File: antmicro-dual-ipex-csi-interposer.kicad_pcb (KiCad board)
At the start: 4 copper layers, 26.5 x 35.5 mm, 18 parts, among them J1 WE_68715014522, J2 MSAK24025P30

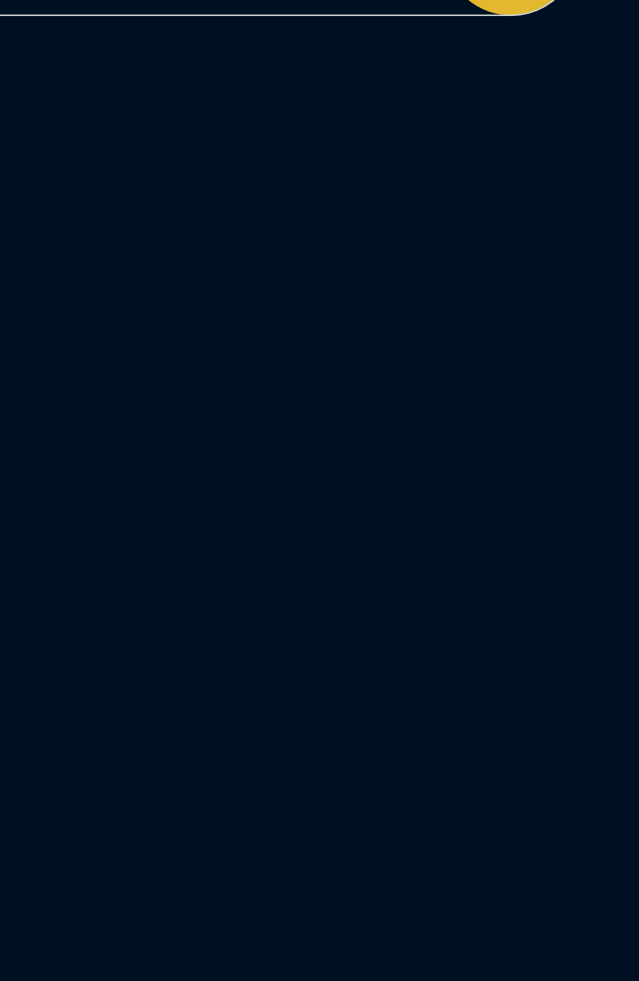
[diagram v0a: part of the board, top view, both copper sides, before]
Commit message: Add second connector and assigned signals
Remove Kicad5 CI
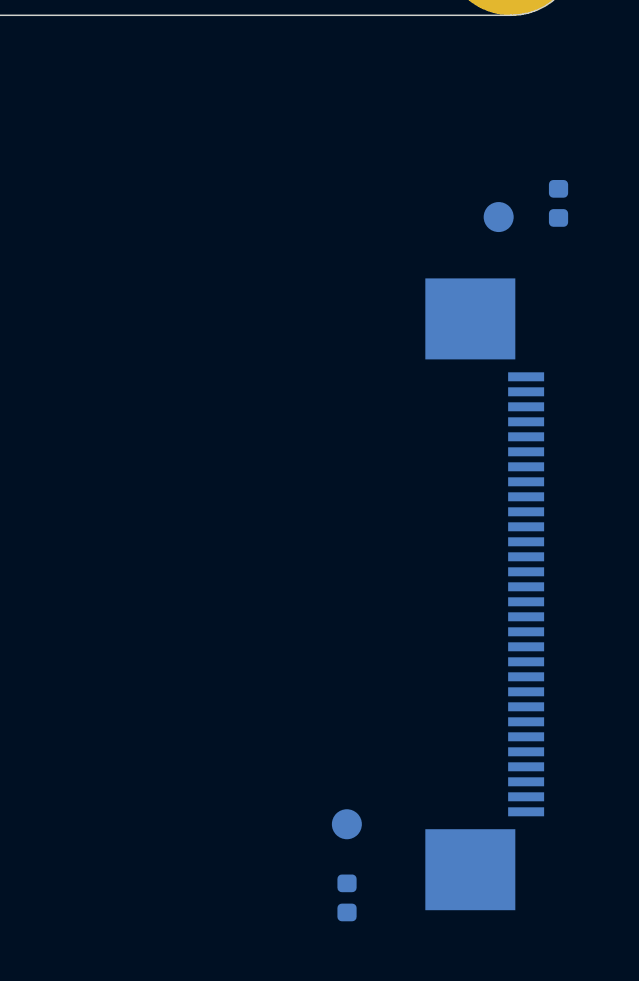
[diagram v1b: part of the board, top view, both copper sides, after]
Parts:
- added J3: MSAK24025P30, antmicro-footprints:MSAK24025P30, B.Cu at (125.4, 154.8)
- added R3: R_0R_0402, antmicro-footprints:0402-res, B.Cu at (118.8, 164.9)
- added R4: R_0R_0402, antmicro-footprints:0402-res, B.Cu at (125.8, 141.8)
- added TP10: TP_SMD1MM, antmicro-footprints:Testpoint_smd_1mm, B.Cu at (123.8, 142.2)
- added TP9: TP_SMD1MM, antmicro-footprints:Testpoint_smd_1mm, B.Cu at (118.7, 162.5)
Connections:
- net CSI_CAM_EN renamed CAM1_CSI_CAM_EN
- net CSI_CAM_XVS renamed CAM1_CSI_CAM_XVS
- net CSI_CLK_N renamed CAM1_CSI_CLK_N
- net CSI_CLK_P renamed CAM1_CSI_CLK_P
- net CSI_D0_N renamed CAM1_CSI_D0_N
- net CSI_D0_P renamed CAM1_CSI_D0_P
- net CSI_D1_N renamed CAM1_CSI_D1_N
- net CSI_D1_P renamed CAM1_CSI_D1_P
- net CSI_D2_N renamed CAM1_CSI_D2_N
- net CSI_D2_P renamed CAM1_CSI_D2_P
- net CSI_D3_N renamed CAM1_CSI_D3_N
- net CSI_D3_P renamed CAM1_CSI_D3_P
- J1 pad 1: unconnected-(J1-Pad1) -> CAM2_CSI_D3_N
- J1 pad 10: unconnected-(J1-Pad10) -> CAM2_CSI_CLK_N
- J1 pad 11: unconnected-(J1-Pad11) -> CAM2_CSI_CLK_P
- J1 pad 2: unconnected-(J1-Pad2) -> CAM2_CSI_D3_P
- J1 pad 3: unconnected-(J1-Pad3) -> CAM2_CSI_D2_N
- J1 pad 4: unconnected-(J1-Pad4) -> CAM2_CSI_D2_P
- J1 pad 5: unconnected-(J1-Pad5) -> CAM2_CSI_D1_N
- J1 pad 6: unconnected-(J1-Pad6) -> CAM2_CSI_D1_P
- J1 pad 7: unconnected-(J1-Pad7) -> CAM2_CSI_D0_N
- J1 pad 8: unconnected-(J1-Pad8) -> CAM2_CSI_D0_P
- J2 pad 22: CSI_CAM_CLK -> CAM1_CSI_CAM_CLK
- J2 pad 23: CSI_CAM_XTRIG -> CAM1_CSI_CAM_XTRIG
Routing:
- net CSI_CAM_XTRIG: track 30.1 -> 0.00 mm
- net CAM1_CSI_CAM_XTRIG: track 0.00 -> 30.1 mm
- net CSI_CAM_CLK: track 28.0 -> 0.00 mm
- net CAM1_CSI_CAM_CLK: track 0.00 -> 28.0 mm

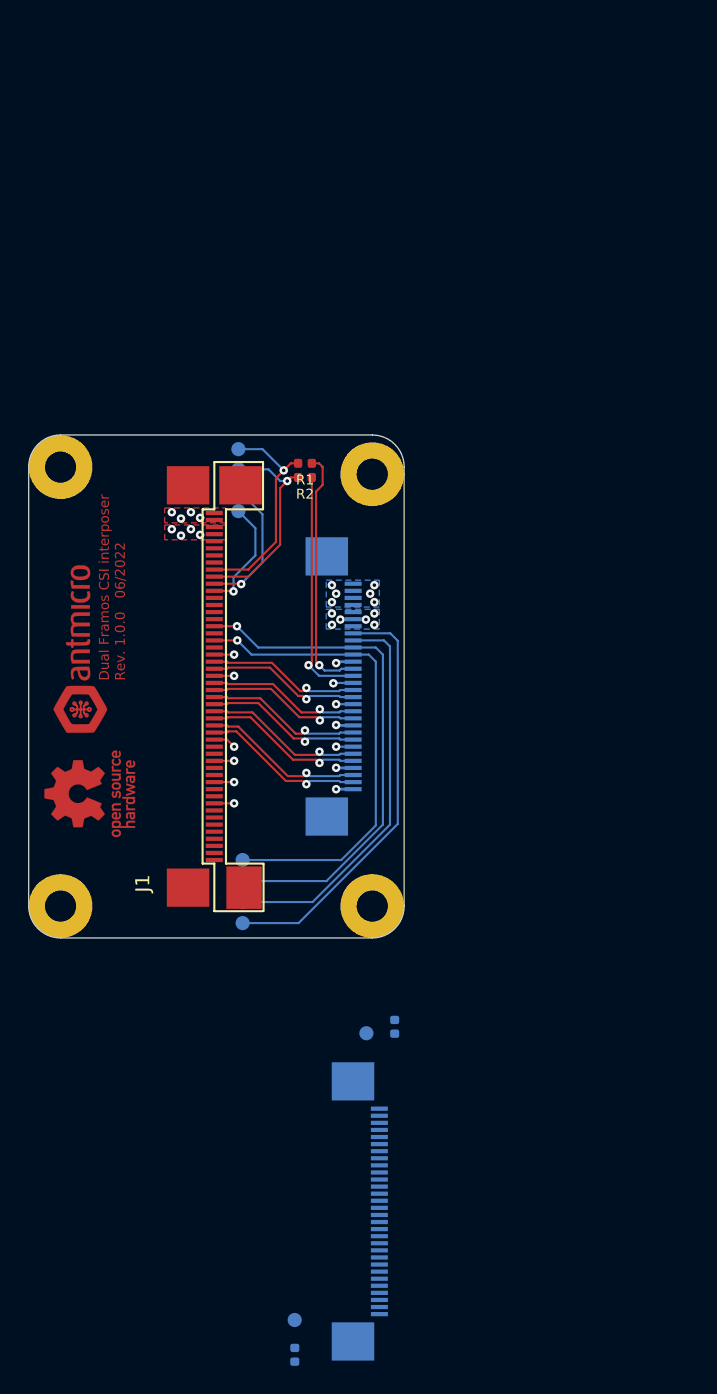
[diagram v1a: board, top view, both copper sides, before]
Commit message: Complete schematic. Proceed PCB layout
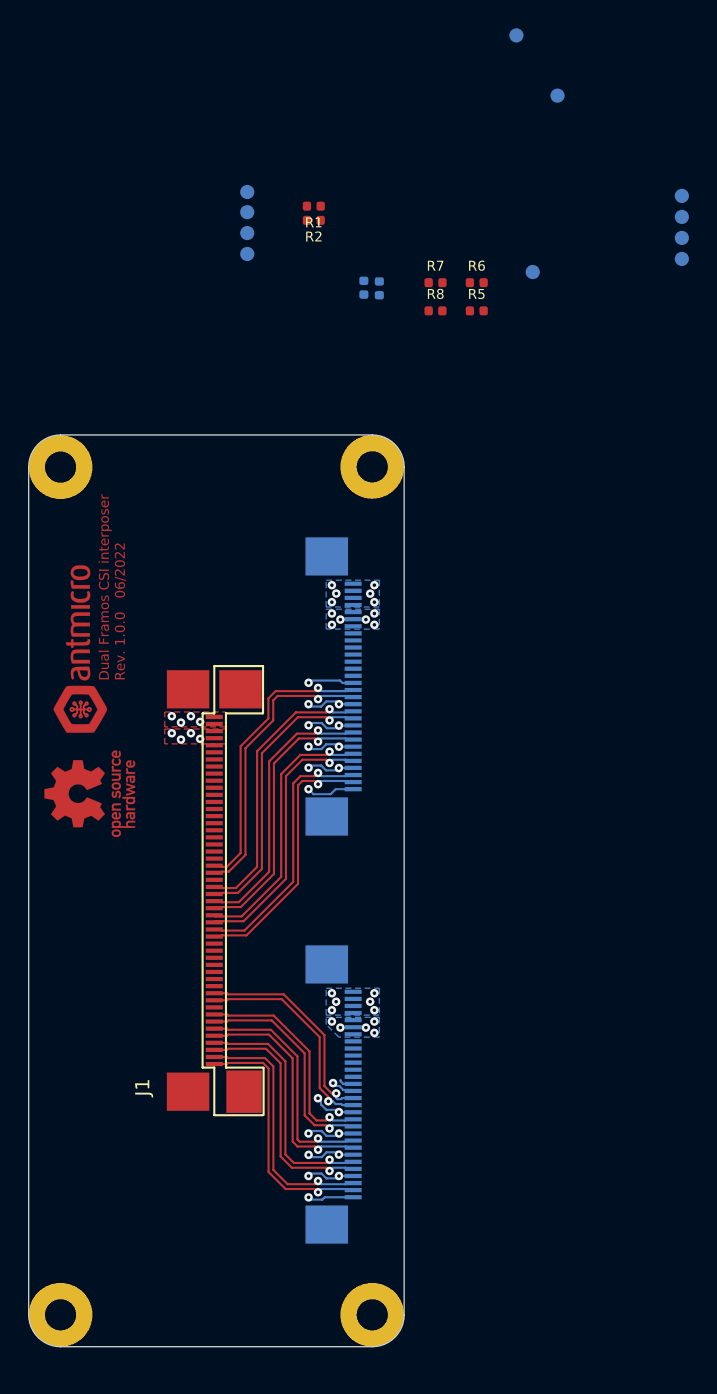
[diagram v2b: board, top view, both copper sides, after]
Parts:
- added R5: R_0R_0402, antmicro-footprints:0402-res, F.Cu at (131.6, 91.2)
- added R6: R_0R_0402, antmicro-footprints:0402-res, F.Cu at (131.6, 89.2)
- added R7: R_0R_0402, antmicro-footprints:0402-res, F.Cu at (128.7, 89.2)
- added R8: R_0R_0402, antmicro-footprints:0402-res, F.Cu at (128.7, 91.2)
- added TP3: TP_SMD1MM, antmicro-footprints:Testpoint_smd_1mm, B.Cu at (134.4, 71.8)
- moved TP9 75.8 mm to (135.5, 88.5)
- moved R3 75.5 mm to (123.7, 89.6)
- moved TP10 67.5 mm to (137.3, 76.0)
- moved TP2 56.2 mm to (146.1, 87.5)
- moved TP8 56.2 mm to (146.1, 84.6)
- moved TP1 56.2 mm to (146.1, 86.0)
- moved TP7 56.2 mm to (146.1, 83.1)
- moved R4 52.1 mm to (124.8, 89.7)
- moved MP2 28.8 mm to (102.2, 162.1)
- moved MP4 28.8 mm to (124.2, 162.1)
- moved R1 18.2 mm to (120.1, 83.8)
- moved R2 18.2 mm to (120.1, 84.8)
- moved TP4 18.2 mm to (115.4, 85.8)
- moved TP3 18.2 mm to (115.4, 87.3)
- moved TP5 18.2 mm to (115.4, 82.9)
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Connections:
- J1 pad 32: CAM1_CSI_CAM_EN -> /CAM_CSI_CAM_EN
- J1 pad 34: CAM1_CSI_CAM_XVS -> /CAM_CSI_CAM_XVS
- J3 pad 20: CAM1_CSI_CAM_EN -> CAM2_CSI_CAM_EN
- J3 pad 21: CAM1_CSI_CAM_XVS -> CAM2_CSI_CAM_XVS
- J3 pad 22: CAM1_CSI_CAM_CLK -> CAM2_CSI_CAM_CLK
- J3 pad 23: CAM1_CSI_CAM_XTRIG -> CAM2_CSI_CAM_XTRIG
- TP7 pad 1: CAM1_CSI_CAM_EN -> /CAM_CSI_CAM_EN
- TP8 pad 1: CAM1_CSI_CAM_XVS -> /CAM_CSI_CAM_XVS
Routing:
- net CAM1_CSI_CAM_XVS: track 36.3 -> 0.00 mm, vias 1 -> 0
- net CAM1_CSI_CAM_EN: track 34.0 -> 0.00 mm, vias 1 -> 0
- net CAM1_CSI_CAM_XTRIG: track 30.1 -> 0.00 mm
- net CAM1_CSI_CAM_CLK: track 28.0 -> 0.00 mm
- net GND: track 17.3 -> 38.7 mm, vias 13 -> 20
- net CAM2_CSI_D3_N: track 0.00 -> 18.0 mm, vias 0 -> 1
- net CAM2_CSI_D3_P: track 0.00 -> 18.0 mm, vias 0 -> 1
- net CAM1_SCL: track 17.8 -> 0.00 mm, vias 1 -> 0
- net CAM2_CSI_D2_N: track 0.00 -> 17.4 mm, vias 0 -> 1
- net CAM2_CSI_D2_P: track 0.00 -> 17.4 mm, vias 0 -> 1
- net CAM1_SDA: track 16.8 -> 0.00 mm, vias 1 -> 0
- net CAM2_CSI_D1_N: track 0.00 -> 16.8 mm, vias 0 -> 1
- net CAM2_CSI_D1_P: track 0.00 -> 16.8 mm, vias 0 -> 1
- net CAM2_CSI_D0_N: track 0.00 -> 15.7 mm, vias 0 -> 1
- net CAM2_CSI_D0_P: track 0.00 -> 15.7 mm, vias 0 -> 1
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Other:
- board size 26.5 x 35.5 mm -> 26.5 x 64.3 mm

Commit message: Route low speed, optimize polygons, match lane length
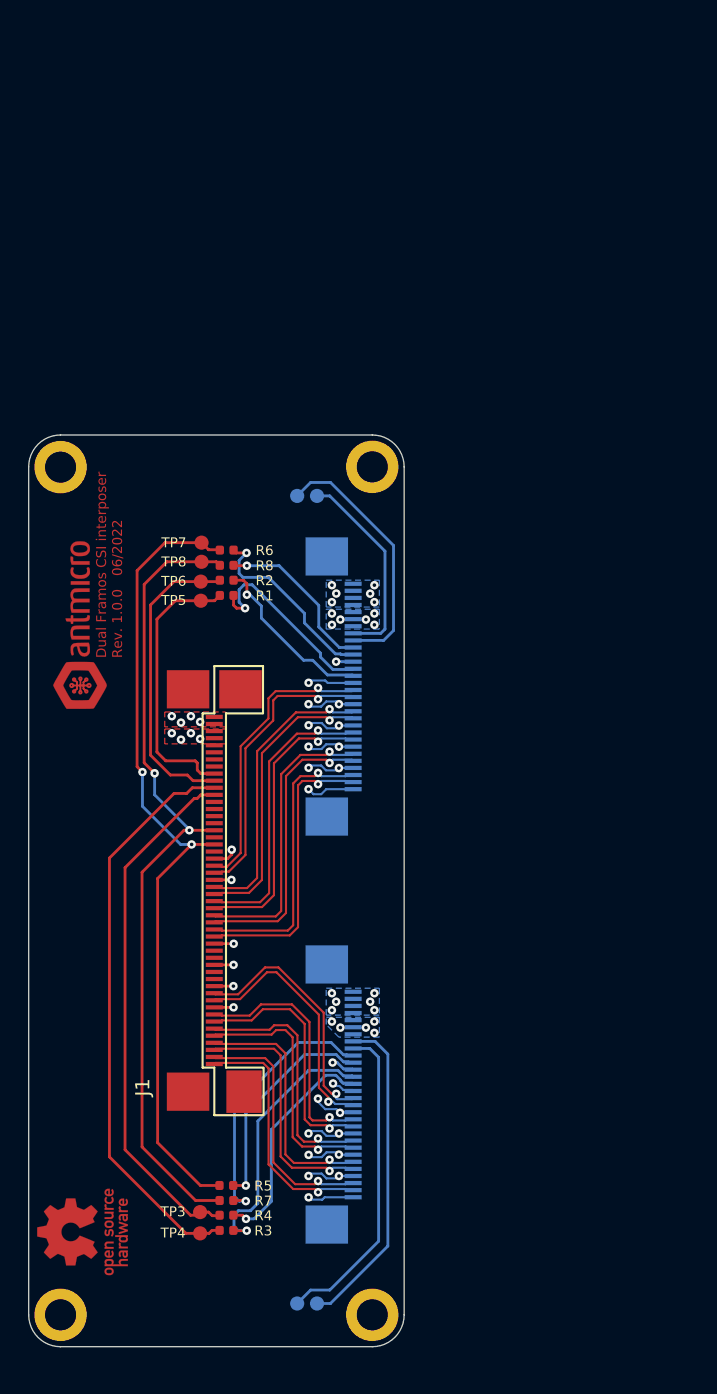
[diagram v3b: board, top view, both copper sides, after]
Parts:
- removed the TP3 at (134.4, 71.8)
- R3, R4, TP3, TP4, TP5, TP6, TP7, TP8: moved to F.Cu
- moved TP10 86.9 mm to (120.3, 161.3)
- moved TP9 74.7 mm to (118.9, 161.3)
- moved TP4 70.7 mm to (112.1, 156.4), turned to 0 degrees
- moved TP3 67.7 mm to (112.1, 154.9), turned to 0 degrees
- moved R3 67.2 mm to (114.0, 156.1), turned to 180 degrees
- moved R7 66.4 mm to (114.0, 154.0), turned to 180 degrees
- moved R4 66.3 mm to (114.0, 155.1), turned to 180 degrees
- moved R5 64.2 mm to (114.0, 153.0), turned to 180 degrees
- moved TP7 41.8 mm to (112.2, 107.5), turned to 180 degrees
- moved TP8 41.7 mm to (112.2, 108.9), turned to 180 degrees
- moved TP1 32.7 mm to (119.0, 104.2)
- moved N1 30.9 mm to (103.8, 156.2)
- moved TP2 30.7 mm to (120.3, 104.2)
- moved TP5 29.0 mm to (112.2, 111.8), turned to 0 degrees
- moved R1 28.2 mm to (114.0, 111.3)
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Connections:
- TP1 pad 1: CSI_CAM_CLK -> CAM1_CSI_CAM_CLK
- TP10 pad 1: CSI_CAM_XTRIG -> CAM2_CSI_CAM_XTRIG
- TP2 pad 1: CSI_CAM_XTRIG -> CAM1_CSI_CAM_XTRIG
- TP9 pad 1: CSI_CAM_CLK -> CAM2_CSI_CAM_CLK
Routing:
- net /CAM_CSI_CAM_XVS: track 0.00 -> 57.5 mm, vias 0 -> 2
- net /CAM_CSI_CAM_EN: track 0.00 -> 57.5 mm, vias 0 -> 2
- net /CAM_L_SCL: track 0.00 -> 40.6 mm
- net /CAM_L_SDA: track 0.00 -> 37.0 mm
- net CAM2_CSI_CAM_XTRIG: track 0.00 -> 23.0 mm
- net CAM2_CSI_CAM_CLK: track 0.00 -> 22.6 mm
- net /CAM_R_SDA: track 0.00 -> 21.5 mm
- net /CAM_R_SCL: track 0.00 -> 19.5 mm
- net CAM2_SCL: track 0.00 -> 19.0 mm, vias 0 -> 1
- net CAM2_CSI_CAM_XVS: track 0.00 -> 18.8 mm, vias 0 -> 1
- net CAM1_CSI_CAM_CLK: track 0.00 -> 18.2 mm
- net CAM2_CSI_CAM_EN: track 0.00 -> 15.5 mm, vias 0 -> 1
- net CAM2_SDA: track 1.06 -> 16.0 mm, vias 0 -> 1
- net CAM1_CSI_CAM_XTRIG: track 0.00 -> 14.3 mm
- net CAM1_SCL: track 0.00 -> 13.9 mm, vias 0 -> 1
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- added copper zone on In2.Cu, net 5V0_SYS

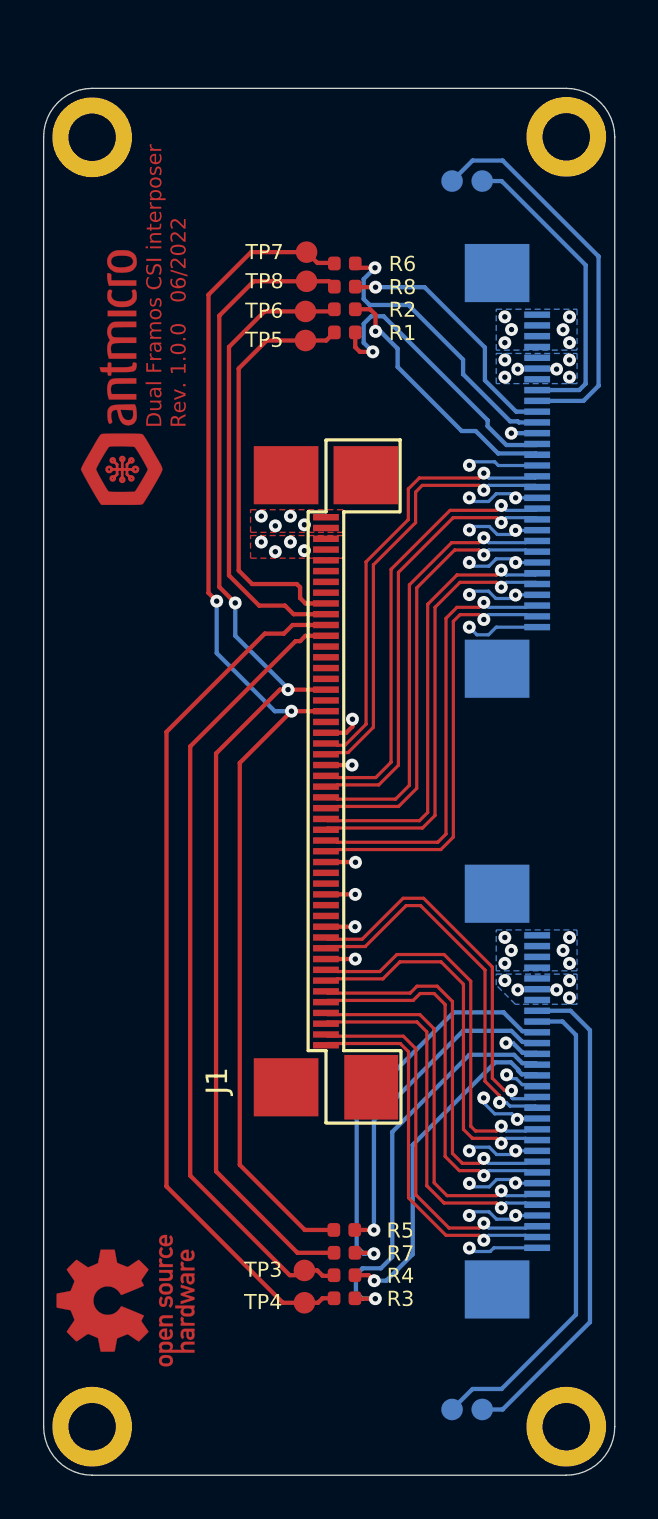
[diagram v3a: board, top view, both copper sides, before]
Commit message: Add decoupling, move all TP to the top
Cosmetic changes

Capital letter fix
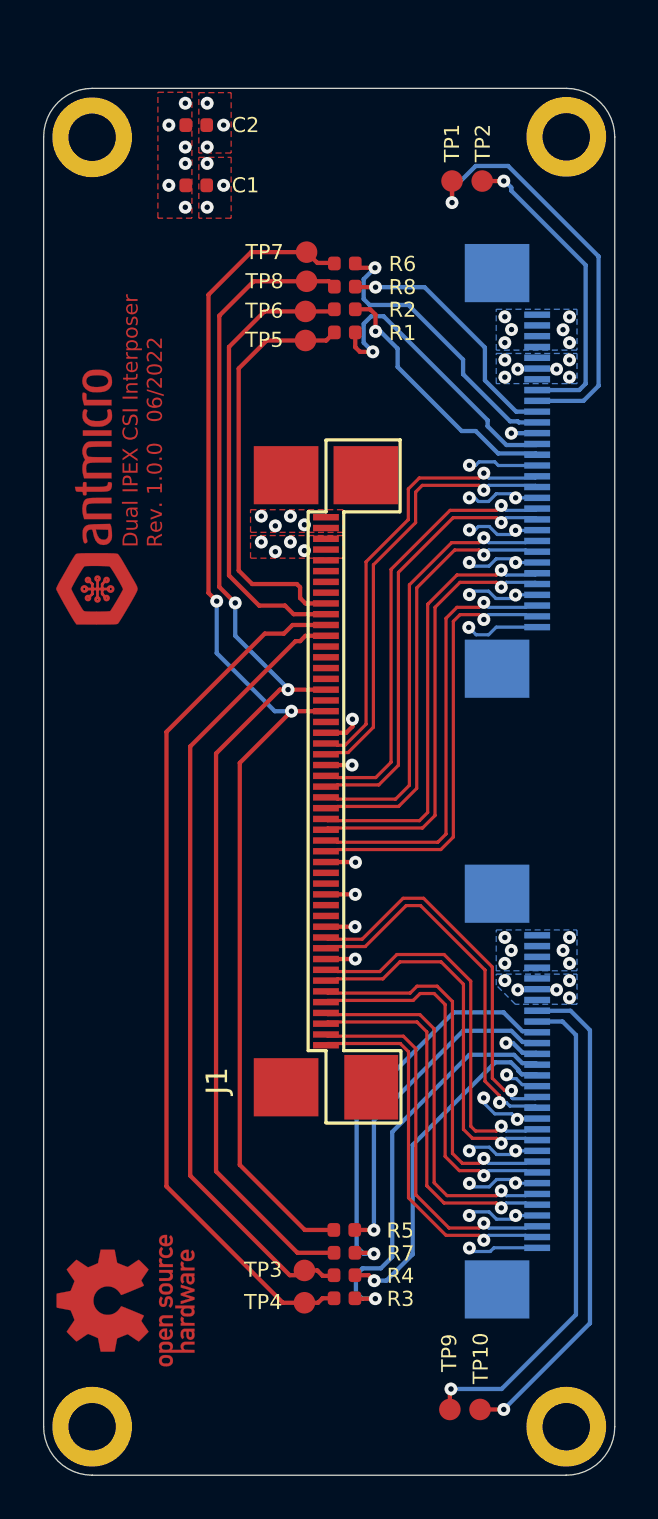
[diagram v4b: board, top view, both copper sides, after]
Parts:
- added C1: C_100n_0402, antmicro-footprints:0402-cap, F.Cu at (107.1, 104.5)
- added C2: C_100n_0402, antmicro-footprints:0402-cap, F.Cu at (107.1, 101.7)
- TP1, TP10, TP2, TP9: moved to F.Cu
- moved N2 5.67 mm to (102.5, 119.0)
- turned TP1 to 180 degrees
- turned TP2 to 180 degrees
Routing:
- net CAM1_CSI_CAM_CLK: track 18.2 -> 19.7 mm, vias 0 -> 1
- net CAM2_CSI_CAM_CLK: track 22.6 -> 23.2 mm, vias 0 -> 1
- net CAM2_CSI_CAM_XTRIG: track 23.0 -> 23.2 mm, vias 0 -> 1
- net CAM1_CSI_CAM_XTRIG: track 14.3 -> 14.4 mm, vias 0 -> 1
- net GND: track 49.9 -> 50.0 mm, vias 28 -> 34
- net 5V0_SYS: vias 16 -> 19
- net 3V3_FFC: vias 15 -> 18
- added copper zone on F.Cu, net GND
- added copper zone on In1.Cu, net GND
- removed copper zone on In1.Cu, net 5V0_SYS
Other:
- board text added: "Dual IPEX CSI Interposer Rev. 1.0.0 06/2022"
- board text removed: "Dual Framos CSI interposer Rev. 1.0.0 06/2022"

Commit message: Generate loclib. Cleanup
Add boards image. Add image link to README
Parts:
- C1, C2: footprint antmicro-footprints:0402-cap -> antmicro-dual-ipex-csi-interposer-footprints:0402-cap
- J1: footprint antmicro-footprints:WE_68715014522 -> antmicro-dual-ipex-csi-interposer-footprints:WE_68715014522
- J2, J3: footprint antmicro-footprints:MSAK24025P30 -> antmicro-dual-ipex-csi-interposer-footprints:MSAK24025P30
- MP1, MP2, MP3, MP4: footprint antmicro-footprints:mounting-hole-2.2mm -> antmicro-dual-ipex-csi-interposer-footprints:mounting-hole-2.2mm
- N1: footprint antmicro-footprints:oshw-logo -> antmicro-dual-ipex-csi-interposer-footprints:oshw-logo
- N2: footprint antmicro-footprints:antmicro-logo_scaled_12mm -> antmicro-dual-ipex-csi-interposer-footprints:antmicro-logo_scaled_12mm
- R1, R2, R3, R4, R5, R6, R7, R8: footprint antmicro-footprints:0402-res -> antmicro-dual-ipex-csi-interposer-footprints:0402-res
- TP1, TP10, TP2, TP3, TP4, TP5, TP6, TP7, TP8, TP9: footprint antmicro-footprints:Testpoint_smd_1mm -> antmicro-dual-ipex-csi-interposer-footprints:Testpoint_smd_1mm
